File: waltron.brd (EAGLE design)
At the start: 53.6 x 47 mm, 21 parts, among them IC1 4049N, U1 LM386

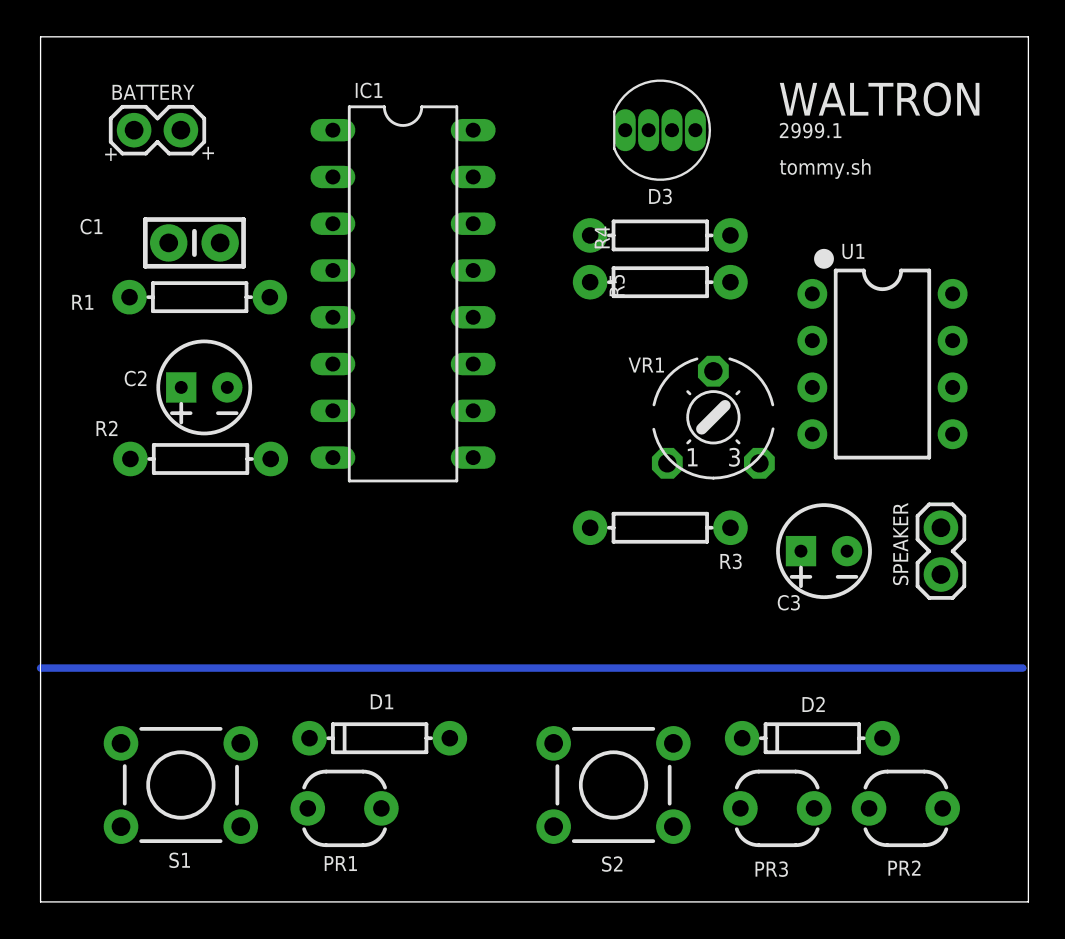
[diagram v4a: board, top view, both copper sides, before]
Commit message: New layout, routed
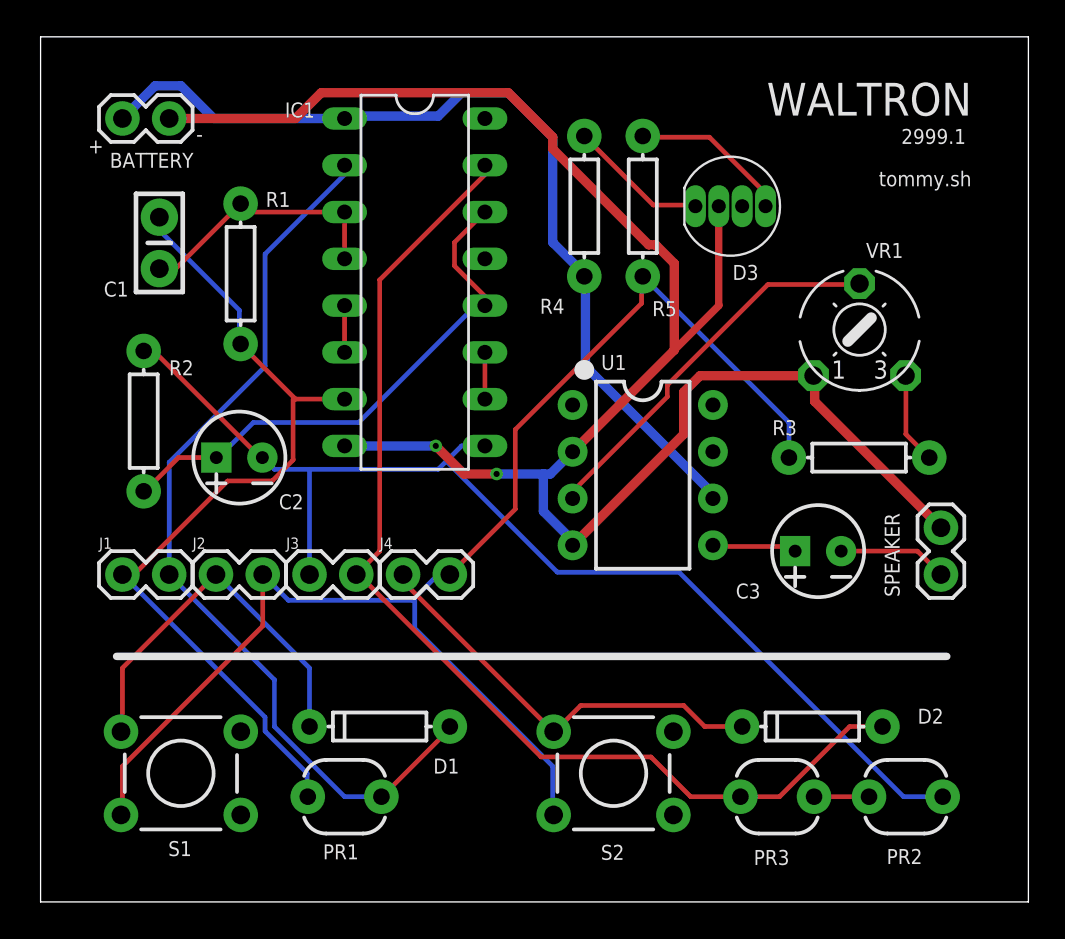
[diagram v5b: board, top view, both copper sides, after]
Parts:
- added J1, J2, J3, J4: (no value), SparkFun-Connectors:1X02
- moved U1 14.3 mm to (32.7, 23.2)
- moved R3 11.4 mm to (44.5, 24.1), turned to 0 degrees
- moved VR1 9.26 mm to (44.5, 31.1)
- moved D3 5.62 mm to (37.5, 37.8)
- moved R4 4.42 mm to (29.5, 37.8), turned to 90 degrees
- moved C2 4.26 mm to (10.8, 24.1)
- moved R5 4.24 mm to (32.7, 37.8), turned to 90 degrees
- moved R2 3.71 mm to (5.60, 26.1), turned to 270 degrees
- moved R1 2.56 mm to (10.9, 34.1), turned to 90 degrees
- moved SPEAKER 2.54 mm to (48.9, 17.8), turned to 90 degrees
- moved C1 1.91 mm to (6.45, 35.8), turned to 270 degrees
- moved BATTERY 0.90 mm to (4.45, 42.5)
- moved IC1 0.90 mm to (20.3, 33.7)
- moved S1 0.64 mm to (7.62, 6.99)
- moved S2 0.64 mm to (31.1, 6.99)
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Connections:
- net N$11: now also J4.1
- net N$12: now also J2.2, J4.2
- net N$3: now also J1.1
- net N$4: now also J1.2
- net N$5: now also J3.1
- net N$8: now also J3.2
- net N$9: now also J2.1
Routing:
- net GND: track 0.00 -> 101.0 mm, vias 0 -> 2
- net N$12: track 0.00 -> 76.1 mm
- net N$5: track 0.00 -> 61.9 mm
- net N$8: track 0.00 -> 60.3 mm
- net N$19: track 53.3 -> 0.00 mm
- net V+: track 0.00 -> 49.6 mm
- net N$4: track 0.00 -> 49.5 mm
- net N$3: track 0.00 -> 47.1 mm
- net N$7: track 0.00 -> 29.1 mm
- net N$11: track 0.00 -> 23.2 mm
- net N$9: track 0.00 -> 21.1 mm
- net N$16: track 0.00 -> 21.0 mm
- net N$2: track 0.00 -> 14.3 mm
- net N$17: track 0.00 -> 8.65 mm
- net N$18: track 0.00 -> 7.65 mm
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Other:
- board text added: "-"
